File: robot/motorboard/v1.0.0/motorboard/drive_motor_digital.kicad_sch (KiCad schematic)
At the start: 13 parts

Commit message: bus name ERC fixes
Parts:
- gave numbers to parts that had none: 13
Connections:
- net SENSE_U renamed SENSE.U
- net SENSE_V renamed SENSE.V
- net SENSE_W renamed SENSE.W
- no-connect marks 0 -> 2
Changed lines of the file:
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@@
   (junction (at 134.62 85.09) (diameter 0.9144) (color 0 0 0 0))
   (junction (at 198.12 82.55) (diameter 0.9144) (color 0 0 0 0))
+  (no_connect (at 193.04 36.83))
+  (no_connect (at 193.04 39.37))
   (bus_entry (at 222.25 128.27) (size 2.54 2.54)
     (stroke (width 0) (type solid) (color 0 0 0 0))
@@
     (effects (font (size 1.27 1.27)) (justify right bottom))
   )
-  (label "SENSE_U" (at 208.28 52.07 180)
-    (effects (font (size 1.27 1.27)) (justify right bottom))
-  )
-  (label "SENSE_V" (at 208.28 54.61 180)
+  (label "SENSE.U" (at 208.28 52.07 180)
+    (effects (font (size 1.27 1.27)) (justify right bottom))
+  )
+  (label "SENSE.V" (at 208.28 54.61 180)
     (effects (font (size 1.27 1.27)) (justify right bottom))
   )
@@
     (effects (font (size 1.27 1.27)) (justify right bottom))
   )
-  (label "SENSE_W" (at 208.28 64.77 180)
+  (label "SENSE.W" (at 208.28 64.77 180)
     (effects (font (size 1.27 1.27)) (justify right bottom))
   )
@@
     (effects (font (size 1.27 1.27)) (justify right bottom))
   )
-  (label "SENSE_U" (at 217.17 128.27 180)
-    (effects (font (size 1.27 1.27)) (justify right bottom))
-  )
-  (label "SENSE_V" (at 217.17 130.81 180)
-    (effects (font (size 1.27 1.27)) (justify right bottom))
-  )
-  (label "SENSE_W" (at 217.17 133.35 180)
+  (label "SENSE.U" (at 217.17 128.27 180)
+    (effects (font (size 1.27 1.27)) (justify right bottom))
+  )
+  (label "SENSE.V" (at 217.17 130.81 180)
+    (effects (font (size 1.27 1.27)) (justify right bottom))
+  )
+  (label "SENSE.W" (at 217.17 133.35 180)
     (effects (font (size 1.27 1.27)) (justify right bottom))
   )
@@
     (effects (font (size 1.27 1.27)) (justify left))
   )
-  (hierarchical_label "Isense" (shape input) (at 227.33 137.16 0)
+  (hierarchical_label "{SENSE}" (shape input) (at 227.33 137.16 0)
     (effects (font (size 1.27 1.27)) (justify left))
   )
   (symbol (lib_id "power:GND") (at 71.12 52.07 0)
     (in_bom yes) (on_board yes)
-    (property "Reference" "#PWR?" (id 0) (at 71.12 58.42 0)
+    (property "Reference" "#PWR0123" (id 0) (at 71.12 58.42 0)
       (effects (font (size 1.27 1.27)) hide)
     )
@@
   (symbol (lib_id "power:GND") (at 71.12 81.28 0)
     (in_bom yes) (on_board yes) (fields_autoplaced)
-    (property "Reference" "#PWR?" (id 0) (at 71.12 87.63 0)
+    (property "Reference" "#PWR0124" (id 0) (at 71.12 87.63 0)
       (effects (font (size 1.27 1.27)) hide)
     )
@@
   (symbol (lib_id "power:GND") (at 96.52 153.67 0)
     (in_bom yes) (on_board yes) (fields_autoplaced)
-    (property "Reference" "#PWR?" (id 0) (at 96.52 160.02 0)
+    (property "Reference" "#PWR0125" (id 0) (at 96.52 160.02 0)
       (effects (font (size 1.27 1.27)) hide)
     )
@@
   (symbol (lib_id "power:GND") (at 96.52 184.15 0)
     (in_bom yes) (on_board yes) (fields_autoplaced)
-    (property "Reference" "#PWR?" (id 0) (at 96.52 190.5 0)
+    (property "Reference" "#PWR0126" (id 0) (at 96.52 190.5 0)
       (effects (font (size 1.27 1.27)) hide)
     )
@@
   (symbol (lib_id "power:GND") (at 120.65 96.52 0)
     (in_bom yes) (on_board yes) (fields_autoplaced)
-    (property "Reference" "#PWR?" (id 0) (at 120.65 102.87 0)
+    (property "Reference" "#PWR0127" (id 0) (at 120.65 102.87 0)
       (effects (font (size 1.27 1.27)) hide)
     )
@@
   (symbol (lib_id "power:GND") (at 177.8 134.62 0)
     (in_bom yes) (on_board yes) (fields_autoplaced)
-    (property "Reference" "#PWR?" (id 0) (at 177.8 140.97 0)
+    (property "Reference" "#PWR0128" (id 0) (at 177.8 140.97 0)
       (effects (font (size 1.27 1.27)) hide)
     )
@@
   (symbol (lib_id "Device:R_US") (at 59.69 137.16 0)
     (in_bom yes) (on_board yes) (fields_autoplaced)
-    (property "Reference" "R?" (id 0) (at 62.23 135.8899 0)
+    (property "Reference" "R41" (id 0) (at 62.23 135.8899 0)
       (effects (font (size 1.27 1.27)) (justify left))
     )
@@
   (symbol (lib_id "Device:R_US") (at 71.12 137.16 0)
     (in_bom yes) (on_board yes) (fields_autoplaced)
-    (property "Reference" "R?" (id 0) (at 73.66 135.8899 0)
+    (property "Reference" "R42" (id 0) (at 73.66 135.8899 0)
       (effects (font (size 1.27 1.27)) (justify left))
     )
@@
   (symbol (lib_id "Device:R_US") (at 82.55 137.16 0)
     (in_bom yes) (on_board yes) (fields_autoplaced)
-    (property "Reference" "R?" (id 0) (at 85.09 135.8899 0)
+    (property "Reference" "R43" (id 0) (at 85.09 135.8899 0)
       (effects (font (size 1.27 1.27)) (justify left))
     )
@@
   (symbol (lib_id "Device:R_US") (at 116.84 41.91 0)
     (in_bom yes) (on_board yes) (fields_autoplaced)
-    (property "Reference" "R?" (id 0) (at 119.38 40.6399 0)
+    (property "Reference" "R44" (id 0) (at 119.38 40.6399 0)
       (effects (font (size 1.27 1.27)) (justify left))
     )
@@
   (symbol (lib_id "Device:R_US") (at 157.48 130.81 90)
     (in_bom yes) (on_board yes) (fields_autoplaced)
-    (property "Reference" "R?" (id 0) (at 157.48 124.46 90))
+    (property "Reference" "R45" (id 0) (at 157.48 124.46 90))
     (property "Value" "1k" (id 1) (at 157.48 127 90))
     (property "Footprint" "" (id 2) (at 157.734 129.794 90)
@@
   (symbol (lib_id "Device:LED") (at 170.18 130.81 180)
     (in_bom yes) (on_board yes) (fields_autoplaced)
-    (property "Reference" "D?" (id 0) (at 170.3705 123.19 0))
+    (property "Reference" "D6" (id 0) (at 170.3705 123.19 0))
     (property "Value" "RED" (id 1) (at 170.3705 125.73 0))
     (property "Footprint" "" (id 2) (at 170.18 130.81 0)
@@
   (symbol (lib_id "Device:C") (at 53.34 43.18 0)
     (in_bom yes) (on_board yes) (fields_autoplaced)
-    (property "Reference" "C?" (id 0) (at 57.15 41.9099 0)
+    (property "Reference" "C15" (id 0) (at 57.15 41.9099 0)
       (effects (font (size 1.27 1.27)) (justify left))
     )
@@
   (symbol (lib_id "Device:C") (at 71.12 43.18 0)
     (in_bom yes) (on_board yes) (fields_autoplaced)
-    (property "Reference" "C?" (id 0) (at 74.93 41.9099 0)
+    (property "Reference" "C16" (id 0) (at 74.93 41.9099 0)
       (effects (font (size 1.27 1.27)) (justify left))
     )
@@
   (symbol (lib_id "Device:C") (at 71.12 74.93 0)
     (in_bom yes) (on_board yes) (fields_autoplaced)
-    (property "Reference" "C?" (id 0) (at 74.93 73.6599 0)
+    (property "Reference" "C17" (id 0) (at 74.93 73.6599 0)
       (effects (font (size 1.27 1.27)) (justify left))
     )
@@
   (symbol (lib_id "Device:C") (at 120.65 72.39 0)
     (in_bom yes) (on_board yes) (fields_autoplaced)
-    (property "Reference" "C?" (id 0) (at 124.46 71.1199 0)
+    (property "Reference" "C18" (id 0) (at 124.46 71.1199 0)
       (effects (font (size 1.27 1.27)) (justify left))
     )
@@
   (symbol (lib_id "Connector:Conn_01x05_Female") (at 102.87 146.05 0)
     (in_bom yes) (on_board yes) (fields_autoplaced)
-    (property "Reference" "J?" (id 0) (at 104.14 144.7799 0)
+    (property "Reference" "J14" (id 0) (at 104.14 144.7799 0)
       (effects (font (size 1.27 1.27)) (justify left))
     )
@@
   (symbol (lib_id "Connector:Conn_01x06_Female") (at 102.87 173.99 0)
     (in_bom yes) (on_board yes) (fields_autoplaced)
-    (property "Reference" "J?" (id 0) (at 104.14 173.9899 0)
+    (property "Reference" "J15" (id 0) (at 104.14 173.9899 0)
       (effects (font (size 1.27 1.27)) (justify left))
     )
@@
   (symbol (lib_id "st_microcontrollers:STSPIN32F0A") (at 165.1 72.39 0)
     (in_bom yes) (on_board yes) (fields_autoplaced)
-    (property "Reference" "U?" (id 0) (at 165.1 29.21 0))
+    (property "Reference" "U6" (id 0) (at 165.1 29.21 0))
     (property "Value" "STSPIN32F0A" (id 1) (at 165.1 31.75 0))
     (property "Footprint" "" (id 2) (at 167.64 72.39 0)

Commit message: passing ERC
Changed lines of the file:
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@@
+    (stroke (width 0) (type solid) (color 0 0 0 0))
+  )
+  (wire (pts (xy 71.12 34.29) (xy 71.12 36.83))
     (stroke (width 0) (type solid) (color 0 0 0 0))
   )
@@
   )
   (wire (pts (xy 71.12 49.53) (xy 71.12 52.07))
+    (stroke (width 0) (type solid) (color 0 0 0 0))
+  )
+  (wire (pts (xy 71.12 66.04) (xy 71.12 68.58))
     (stroke (width 0) (type solid) (color 0 0 0 0))
   )
@@
     (effects (font (size 1.27 1.27)) (justify left))
   )
+  (symbol (lib_id "power:PWR_FLAG") (at 71.12 34.29 0)
+    (in_bom yes) (on_board yes) (fields_autoplaced)
+    (property "Reference" "#FLG012" (id 0) (at 71.12 32.385 0)
+      (effects (font (size 1.27 1.27)) hide)
+    )
+    (property "Value" "PWR_FLAG" (id 1) (at 71.12 29.21 0))
+    (property "Footprint" "" (id 2) (at 71.12 34.29 0)
+      (effects (font (size 1.27 1.27)) hide)
+    )
+    (property "Datasheet" "~" (id 3) (at 71.12 34.29 0)
+      (effects (font (size 1.27 1.27)) hide)
+    )
+    (pin "1")
+  )
+  (symbol (lib_id "power:PWR_FLAG") (at 71.12 66.04 0)
+    (in_bom yes) (on_board yes) (fields_autoplaced)
+    (property "Reference" "#FLG013" (id 0) (at 71.12 64.135 0)
+      (effects (font (size 1.27 1.27)) hide)
+    )
+    (property "Value" "PWR_FLAG" (id 1) (at 71.12 60.96 0))
+    (property "Footprint" "" (id 2) (at 71.12 66.04 0)
+      (effects (font (size 1.27 1.27)) hide)
+    )
+    (property "Datasheet" "~" (id 3) (at 71.12 66.04 0)
+      (effects (font (size 1.27 1.27)) hide)
+    )
+    (pin "1")
+  )
   (symbol (lib_id "power:GND") (at 71.12 52.07 0)

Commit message: capacitor footprint assn
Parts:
- C15: value 1uF 6.3V -> 1uF; footprint (none) -> Capacitor_SMD:C_0603_1608Metric_Pad1.08x0.95mm_HandSolder
- C16, C17: value 0.1uF 6.3V -> 0.1uF; footprint (none) -> Capacitor_SMD:C_0402_1005Metric_Pad0.74x0.62mm_HandSolder
- C18: footprint (none) -> Capacitor_SMD:C_0603_1608Metric_Pad1.08x0.95mm_HandSolder
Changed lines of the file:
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@@
   (symbol (lib_id "power:PWR_FLAG") (at 71.12 34.29 0)
     (in_bom yes) (on_board yes) (fields_autoplaced)
-    (property "Reference" "#FLG012" (id 0) (at 71.12 32.385 0)
+    (property "Reference" "#FLG03" (id 0) (at 71.12 32.385 0)
       (effects (font (size 1.27 1.27)) hide)
     )
@@
   (symbol (lib_id "power:PWR_FLAG") (at 71.12 66.04 0)
     (in_bom yes) (on_board yes) (fields_autoplaced)
-    (property "Reference" "#FLG013" (id 0) (at 71.12 64.135 0)
+    (property "Reference" "#FLG04" (id 0) (at 71.12 64.135 0)
       (effects (font (size 1.27 1.27)) hide)
     )
@@
   (symbol (lib_id "power:GND") (at 71.12 52.07 0)
     (in_bom yes) (on_board yes)
-    (property "Reference" "#PWR0123" (id 0) (at 71.12 58.42 0)
+    (property "Reference" "#PWR063" (id 0) (at 71.12 58.42 0)
       (effects (font (size 1.27 1.27)) hide)
     )
@@
   (symbol (lib_id "power:GND") (at 71.12 81.28 0)
     (in_bom yes) (on_board yes) (fields_autoplaced)
-    (property "Reference" "#PWR0124" (id 0) (at 71.12 87.63 0)
+    (property "Reference" "#PWR064" (id 0) (at 71.12 87.63 0)
       (effects (font (size 1.27 1.27)) hide)
     )
@@
   (symbol (lib_id "power:GND") (at 96.52 153.67 0)
     (in_bom yes) (on_board yes) (fields_autoplaced)
-    (property "Reference" "#PWR0125" (id 0) (at 96.52 160.02 0)
+    (property "Reference" "#PWR065" (id 0) (at 96.52 160.02 0)
       (effects (font (size 1.27 1.27)) hide)
     )
@@
   (symbol (lib_id "power:GND") (at 96.52 184.15 0)
     (in_bom yes) (on_board yes) (fields_autoplaced)
-    (property "Reference" "#PWR0126" (id 0) (at 96.52 190.5 0)
+    (property "Reference" "#PWR066" (id 0) (at 96.52 190.5 0)
       (effects (font (size 1.27 1.27)) hide)
     )
@@
   (symbol (lib_id "power:GND") (at 120.65 96.52 0)
     (in_bom yes) (on_board yes) (fields_autoplaced)
-    (property "Reference" "#PWR0127" (id 0) (at 120.65 102.87 0)
+    (property "Reference" "#PWR067" (id 0) (at 120.65 102.87 0)
       (effects (font (size 1.27 1.27)) hide)
     )
@@
   (symbol (lib_id "power:GND") (at 177.8 134.62 0)
     (in_bom yes) (on_board yes) (fields_autoplaced)
-    (property "Reference" "#PWR0128" (id 0) (at 177.8 140.97 0)
+    (property "Reference" "#PWR068" (id 0) (at 177.8 140.97 0)
       (effects (font (size 1.27 1.27)) hide)
     )
@@
       (effects (font (size 1.27 1.27)) (justify left))
     )
-    (property "Value" "1uF 6.3V" (id 1) (at 57.15 44.4499 0)
-      (effects (font (size 1.27 1.27)) (justify left))
-    )
-    (property "Footprint" "" (id 2) (at 54.3052 46.99 0)
+    (property "Value" "1uF" (id 1) (at 57.15 44.4499 0)
+      (effects (font (size 1.27 1.27)) (justify left))
+    )
+    (property "Footprint" "Capacitor_SMD:C_0603_1608Metric_Pad1.08x0.95mm_HandSolder" (id 2) (at 54.3052 46.99 0)
       (effects (font (size 1.27 1.27)) hide)
     )
@@
       (effects (font (size 1.27 1.27)) (justify left))
     )
-    (property "Value" "0.1uF 6.3V" (id 1) (at 74.93 44.4499 0)
-      (effects (font (size 1.27 1.27)) (justify left))
-    )
-    (property "Footprint" "" (id 2) (at 72.0852 46.99 0)
+    (property "Value" "0.1uF" (id 1) (at 74.93 44.4499 0)
+      (effects (font (size 1.27 1.27)) (justify left))
+    )
+    (property "Footprint" "Capacitor_SMD:C_0402_1005Metric_Pad0.74x0.62mm_HandSolder" (id 2) (at 72.0852 46.99 0)
       (effects (font (size 1.27 1.27)) hide)
     )
@@
       (effects (font (size 1.27 1.27)) (justify left))
     )
-    (property "Value" "0.1uF 6.3V" (id 1) (at 74.93 76.1999 0)
-      (effects (font (size 1.27 1.27)) (justify left))
-    )
-    (property "Footprint" "" (id 2) (at 72.0852 78.74 0)
+    (property "Value" "0.1uF" (id 1) (at 74.93 76.1999 0)
+      (effects (font (size 1.27 1.27)) (justify left))
+    )
+    (property "Footprint" "Capacitor_SMD:C_0402_1005Metric_Pad0.74x0.62mm_HandSolder" (id 2) (at 72.0852 78.74 0)
       (effects (font (size 1.27 1.27)) hide)
     )
@@
       (effects (font (size 1.27 1.27)) (justify left))
     )
-    (property "Footprint" "" (id 2) (at 121.6152 76.2 0)
-      (effects (font (size 1.27 1.27)) hide)
-    )
+    (property "Footprint" "Capacitor_SMD:C_0603_1608Metric_Pad1.08x0.95mm_HandSolder" (id 2) (at 121.6152 76.2 0)
+      (effects (font (size 1.27 1.27)) hide)
+    )

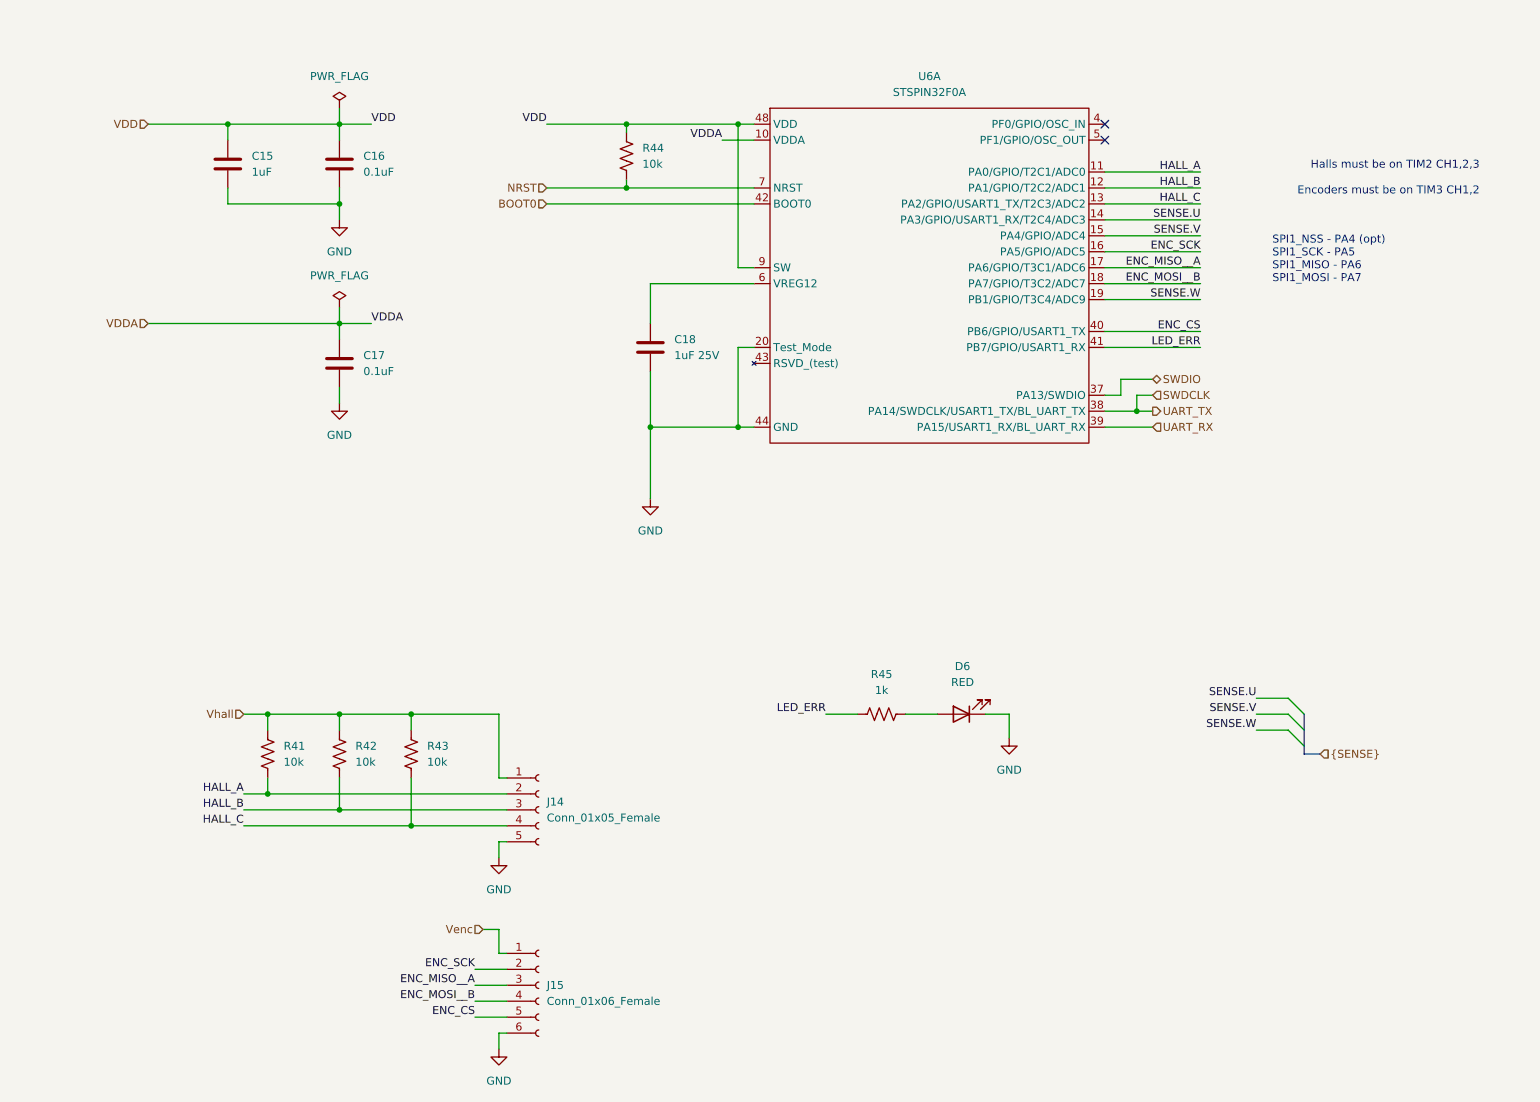
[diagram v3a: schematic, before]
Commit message: cleaned up remaining schematics
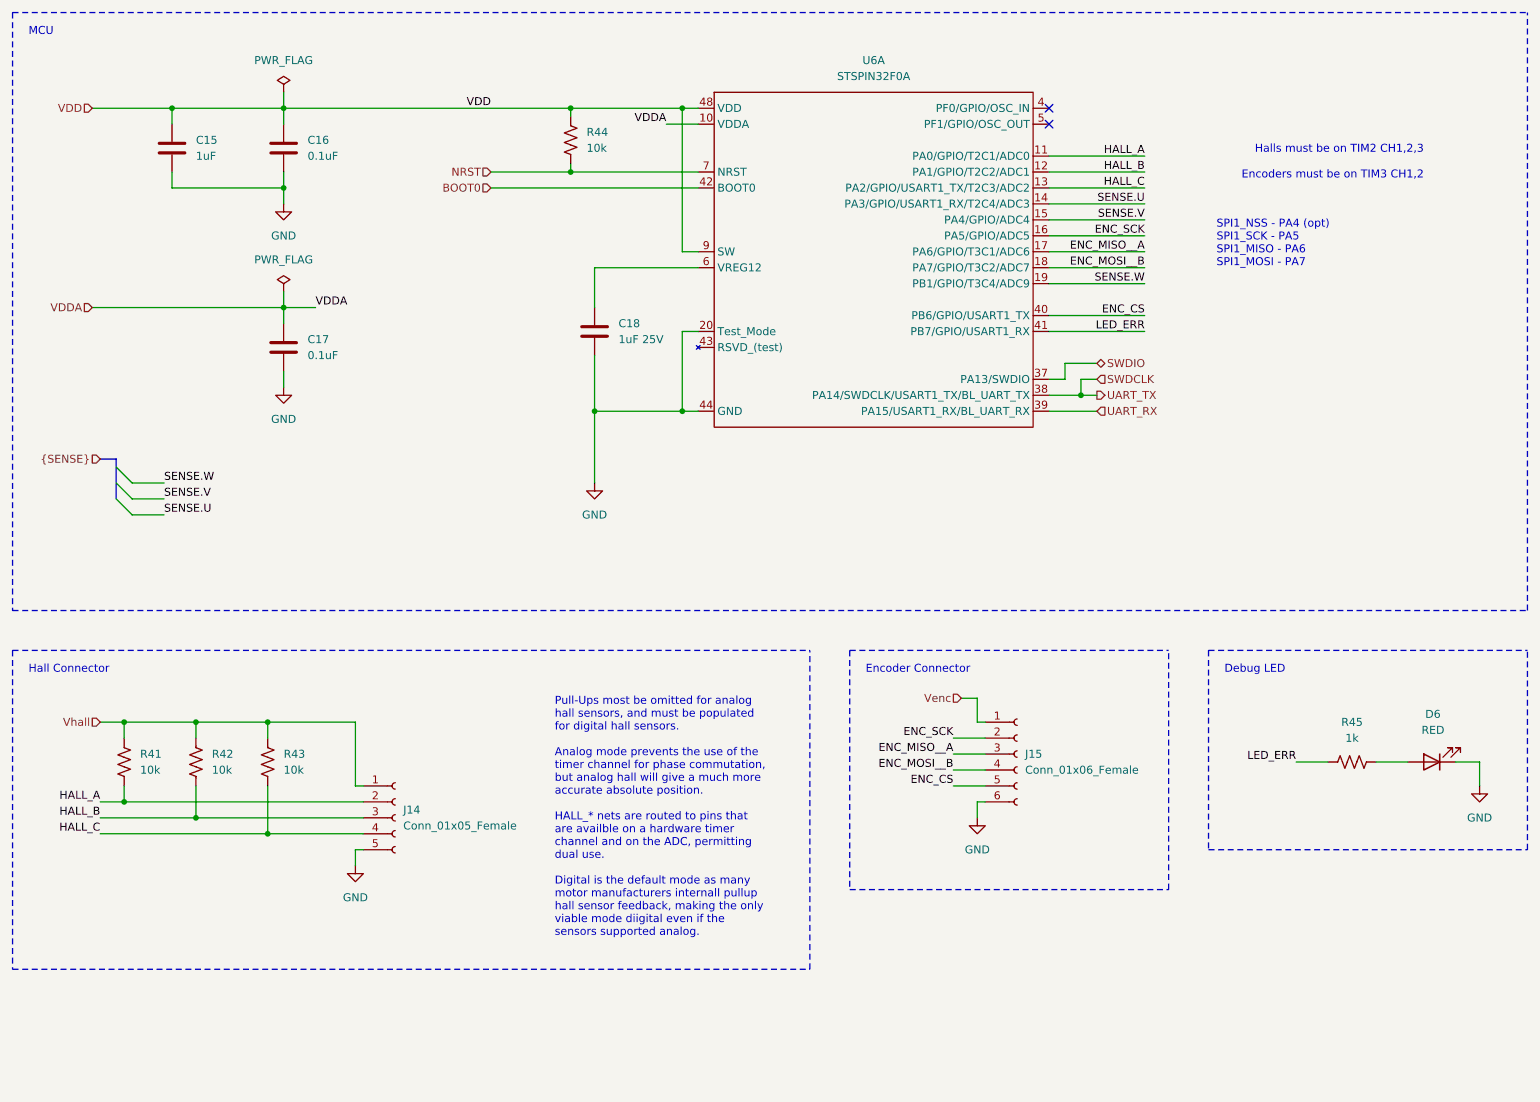
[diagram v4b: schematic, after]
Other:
- note added: "Debug LED"
- note added: "Encoder Connector"
- note added: "Hall Connector"
- note added: "MCU"
- note added: "Pull-Ups most be omitted for analog hall sensors, and must be populated for digital hall sensors. Analog mode prevents the use of the timer channel for phase commutation, but analog hall will give a much more accurate absolute position. HALL_* nets are routed to pins that are availble on a hardware timer channel and on the ADC, permitting dual use. Digital is the default mode as many motor manufa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"
- moved on the sheet: C15, C16, C17, C18, D6, J14, J15, R41, R42, R43, R44, R45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

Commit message: updated title block
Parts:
- C18: value 1uF 25V -> 1uF
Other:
- company: (none) -> The A-Team (RC SSL)
- title: (none) -> Motorboard
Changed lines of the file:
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@@
 (kicad_sch (version 20210621) (generator eeschema)
   (paper "A")
+  (title_block
+    (title "Motorboard")
+    (date "2021-11-14")
+    (rev "1.0.0")
+    (company "The A-Team (RC SSL)")
+    (comment 1 "Designed By: W. Stuckey & R. Osawa")
+    (comment 2 "Reviewed By:")
+  )
   (junction (at 36.83 132.08) (diameter 0.9144) (color 0 0 0 0))
   (junction (at 36.83 144.78) (diameter 0.9144) (color 0 0 0 0))
@@
       (effects (font (size 1.27 1.27)) (justify left))
     )
-    (property "Value" "1uF 25V" (id 1) (at 115.57 71.1199 0)
-      (effects (font (size 1.27 1.27)) (justify left))
-    )
+    (property "Value" "1uF" (id 1) (at 115.57 71.1199 0)
+      (effects (font (size 1.27 1.27)) (justify left))
+    )
